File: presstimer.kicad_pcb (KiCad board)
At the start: 4 copper layers, 93 x 72 mm, 87 parts, among them J1 Screw_Terminal_01x02, J10 Screw_Terminal_01x02, J11 Connector, USB-TYPE-C-16P, J2 Screw_Terminal_01x03, J3 Connector, USB-TYPE-C-16P, J4 Conn_ARM_SWD_TagConnect_TC2030, J5 Conn_01x06_Pin, J6 Conn_01x06_Pin, J8 Screw_Terminal_01x02, J9 Screw_Terminal_01x02, Q10 L8050QLT1G, Q5 Display 2.8" TFT LCD Touch IL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, Q6 AO3401A, Q8 L8050QLT1G, Q9 L8050QLT1G, SW1 SW_Push, SW2 SW_Push, U1 AP7361C-33ER, U2 ESP32-S3-WROOM-1, U3 SFH620A-3X001, U4 SFH620A-3X001, U5 SSR-41FDD, U6 CP2102N-Axx-xQFN28

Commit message: fix: corrected 3v3 connections at D5, USB power to LDO, power to I2C expansion
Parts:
- renumbered TP2 to 3V3, TP1 to 5V, TP4 to 5V, TP6 to 5V, SW1 to BOOT, TP7 to GND, TP3 to GND, TP5 to GND, SW2 to RESET
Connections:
- C10 pad 1: USB2_5V -> +5V
- C11 pad 1: USB_5V -> +5V
- C2 pad 1: Net-(D1-A) -> +3V3
- D1 pad 1: +3V3 -> Net-(D1-K)
- D1 pad 2: Net-(D1-A) -> +3V3
- D5 pad 1: USB_5V -> +5V
- D6 pad 1: USB2_5V -> +5V
- R3 pad 1: +3V3 -> Net-(D1-K)
- U1 pad 2: Net-(D1-A) -> +3V3
- U1 pad 4: Net-(D1-A) -> +3V3
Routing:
- net +5V: track 76.5 -> 172.6 mm, vias 1 -> 7
- net +3V3: track 221.8 -> 258.7 mm
- net Net-(D1-A): track 15.5 -> 0.00 mm
- net VBUSB2: track 21.0 -> 16.7 mm
- net Net-(D1-K): track 0.00 -> 2.36 mm
- net USB_5V: track 2.29 -> 0.00 mm
- net USB2_5V: track 2.26 -> 0.00 mm

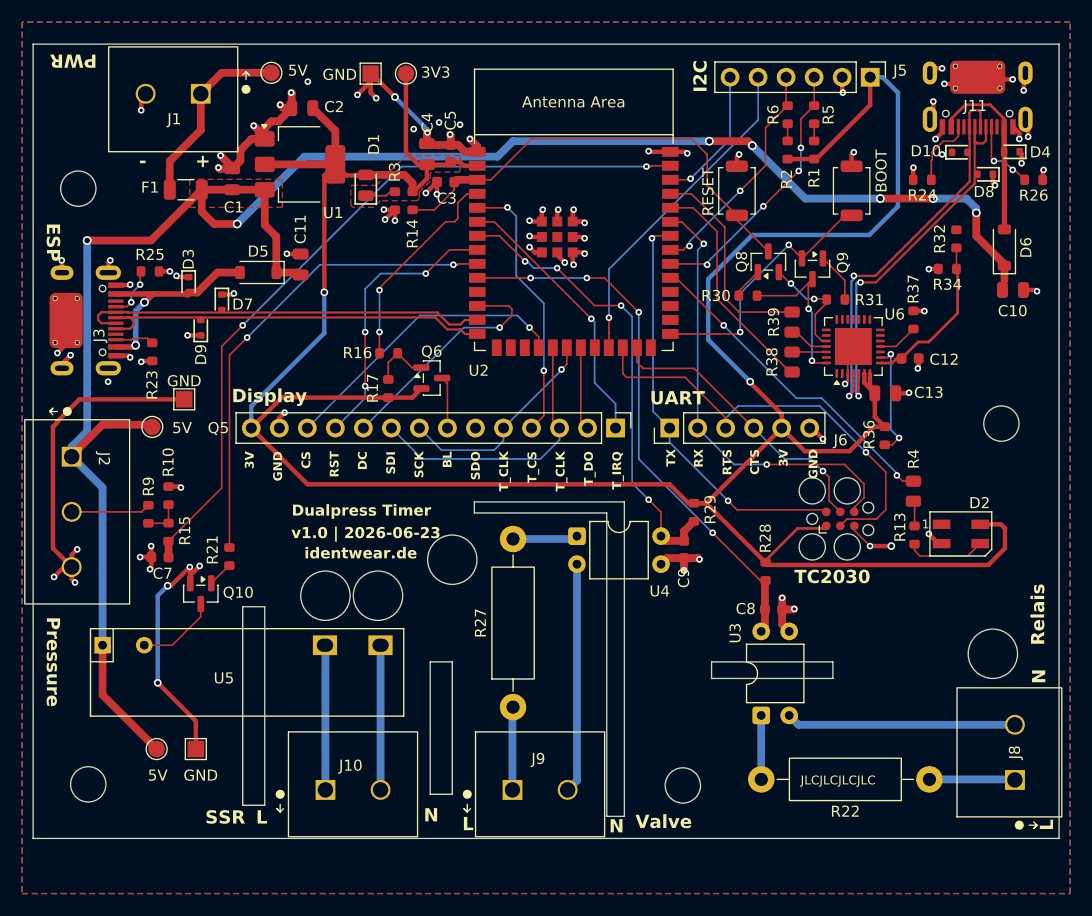
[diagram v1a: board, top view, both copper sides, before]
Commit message: fixed ssr pinout
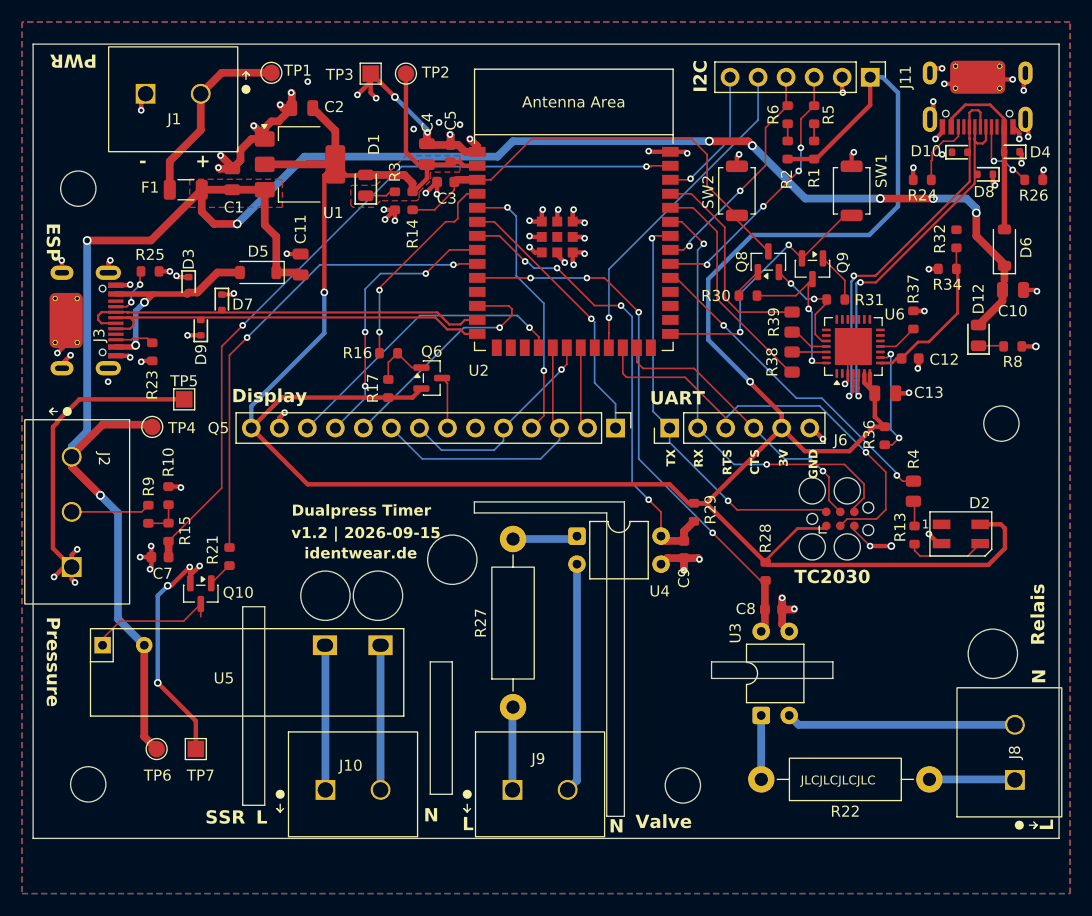
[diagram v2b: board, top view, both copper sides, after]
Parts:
- added D12: LED, PCM_JLCPCB:D_0805, F.Cu at (184.7, 106.4)
- added R8: 1k, PCM_JLCPCB:R_0603, F.Cu at (187.8, 107.4)
- renumbered BOOT to SW1, RESET to SW2, 5V to TP1, 3V3 to TP2, GND to TP3, 5V to TP4, GND to TP5, 5V to TP6, GND to TP7
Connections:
- U5 pad 1: +5V -> Net-(J10-Pin_1)
- U5 pad 2: Net-(Q10-C) -> Net-(J10-Pin_2)
- U5 pad 3: Net-(J10-Pin_1) -> +5V
- U5 pad 4: Net-(J10-Pin_2) -> Net-(Q10-C)
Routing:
- net Net-(Q10-C): track 7.35 -> 11.9 mm
- net +5V: track 172.6 -> 176.7 mm, vias 7 -> 8
- net Net-(D12-K): track 0.00 -> 2.30 mm
- net GND: track 186.8 -> 188.1 mm, vias 89 -> 90
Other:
- board text added: "v1.2 | 2026-09-15"
- board text added: "зайка"
- board text removed: "v1.0 | 2026-06-23"

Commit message: before removal of cp2102
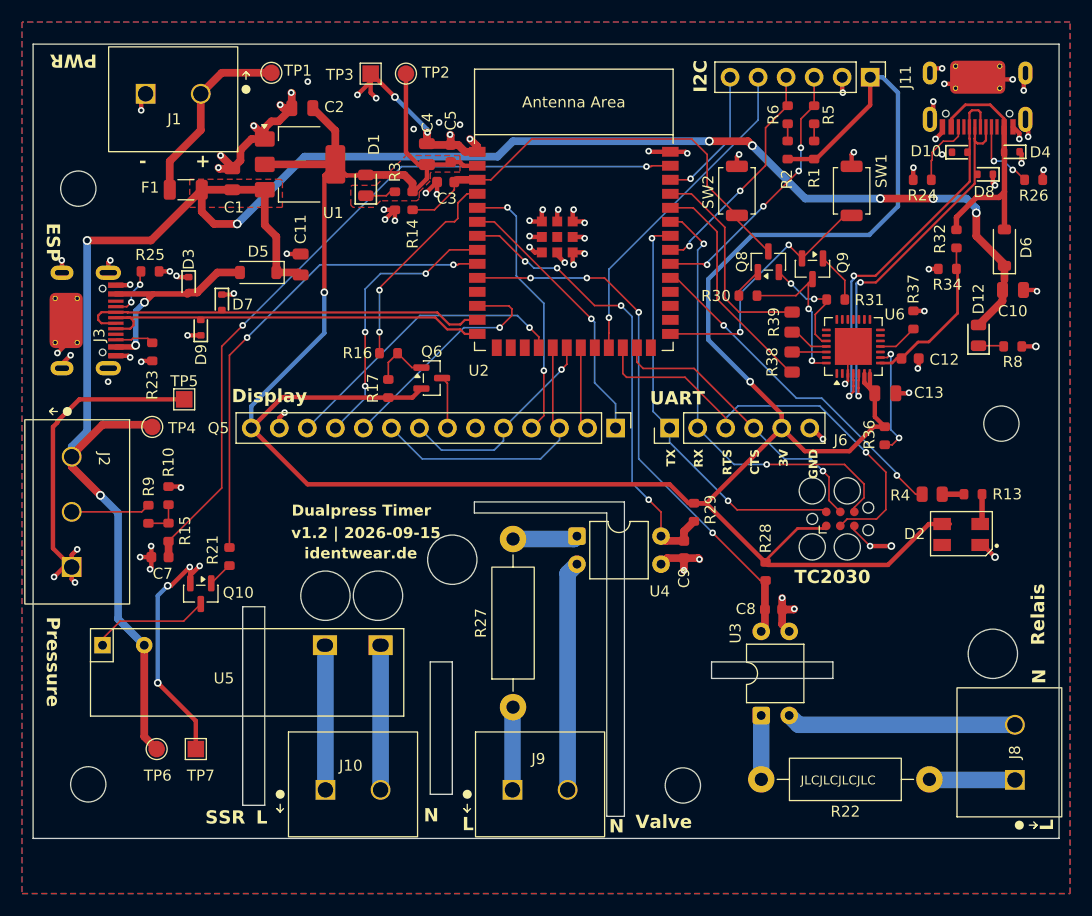
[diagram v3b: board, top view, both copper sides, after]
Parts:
- D2: footprint LED_SMD:LED_SK6812MINI_PLCC4_3.5x3.5mm_P1.75mm -> markus:SK6812MINI--HS-012_3.7x3.5mm
- moved R13 6.46 mm to (184.2, 120.8), turned to 0 degrees
- moved D2 1.92 mm to (181.4, 123.5)
- moved R4 1.72 mm to (180.5, 120.8), turned to 0 degrees
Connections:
- D2 pad 1: unconnected-(D2-DOUT-Pad1) -> GND
- D2 pad 2: GND -> Net-(D2-DIN)
- D2 pad 3: Net-(D2-DIN) -> +3V3
- D2 pad 4: +3V3 -> unconnected-(D2-DOUT-Pad4)
- U5 pad 1: Net-(J10-Pin_1) -> Net-(J10-Pin_2)
- U5 pad 2: Net-(J10-Pin_2) -> Net-(J10-Pin_1)
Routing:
- net +3V3: track 258.7 -> 250.4 mm
- net VBUSB2: track 16.7 -> 23.1 mm
- net Net-(D2-DIN): track 7.20 -> 2.98 mm
- net LED_RGB: track 29.8 -> 31.1 mm
- net Net-(Q10-C): track 11.9 -> 10.8 mm
- net GND: track 188.1 -> 188.7 mm

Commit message: add: connector heating SSR
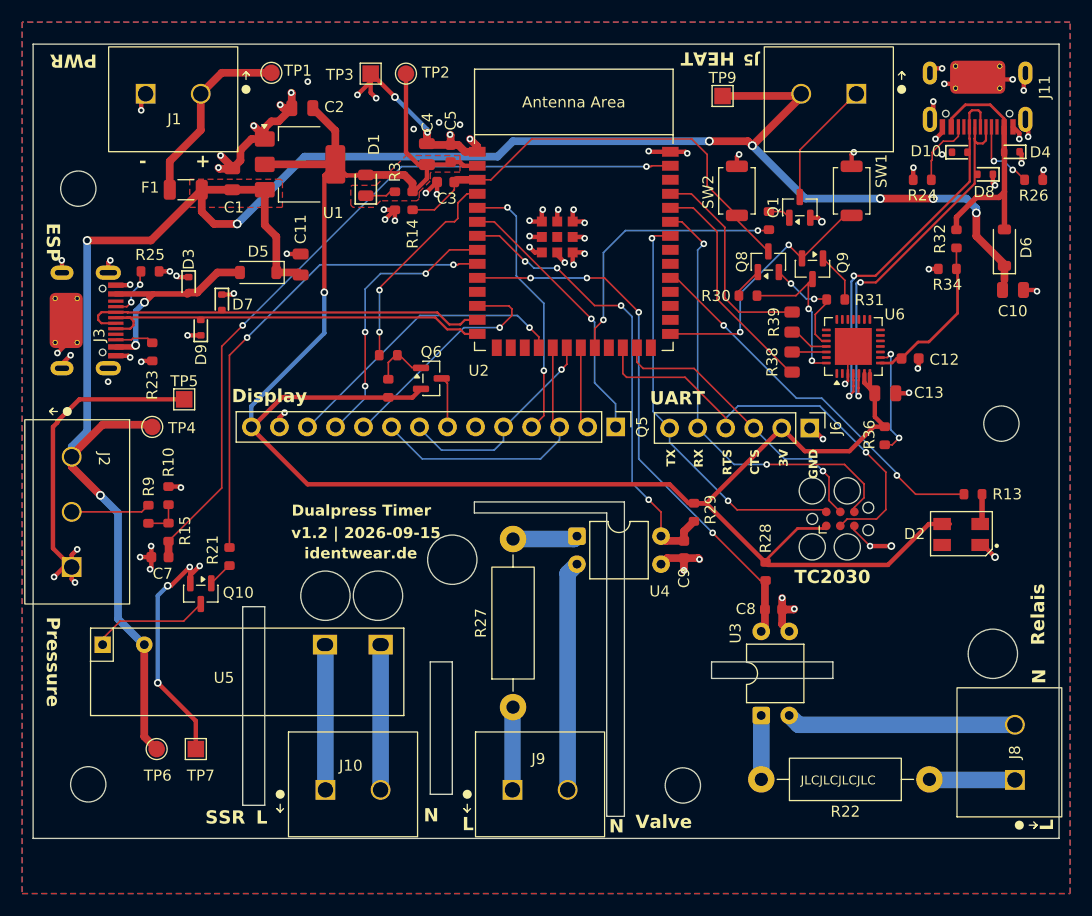
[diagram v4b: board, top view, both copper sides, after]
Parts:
- removed D12: LED, PCM_JLCPCB:D_0805
- removed R2: 4k7, PCM_JLCPCB:R_0603
- removed R37: 10k, PCM_JLCPCB:R_0603
- removed R4: 0, PCM_JLCPCB:R_0805
- removed R5, R6: 0, PCM_JLCPCB:R_0603
- removed R8: 1k, PCM_JLCPCB:R_0603
- added Q1: L8050QLT1G, Package_TO_SOT_SMD:SOT-23, F.Cu at (168.5, 94.8)
- added TP9: TestPoint, TestPoint:TestPoint_Pad_1.5x1.5mm, F.Cu at (161.5, 84.7)
- J5: value Conn_01x06_Pin -> Screw_Terminal_01x02; footprint Connector_PinHeader_2.54mm:PinHeader_1x06_P2.54mm_Vertical -> markus:DG305-5.0-02P-12-00A(H)
- R1: value 4k7 -> 1k
- U5: value SSR-41FDD -> SSR-41FDA
- moved J6 12.7 mm to (169.4, 114.8), turned to -90 degrees
- moved R1 7.60 mm to (165.7, 96.0), turned to 90 degrees
- moved J5 6.76 mm to (176.7, 89.5), turned to 180 degrees
- moved R16 0.18 mm to (131.2, 108.2)
- moved Q5 0.10 mm to (151.8, 114.7)
- moved U5 0.05 mm to (105.3, 134.4)
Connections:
- net Net-(J10-Pin_1) renamed /Connections/SSR_L
- net Net-(J10-Pin_2) renamed /Connections/SSR_SW_L
- net Net-(J8-Pin_1) renamed /Connections/SENSE_RELAY1
- net Net-(J8-Pin_2) renamed /Connections/SENSE_RELAY2
- net Net-(J9-Pin_1) renamed /Connections/SENSE_SOLENOID1
- net Net-(J9-Pin_2) renamed /Connections/SENSE_SOLENOID2
- J5 pad 1: +3V3 -> Net-(J5-Pin_1)
- J5 pad 2: GND -> +5V
- J6 pad 1: UART_TX -> GND
- J6 pad 2: UART_RX -> +3V3
- J6 pad 3: UART_RTS -> UART_CTS
- J6 pad 4: UART_CTS -> UART_RTS
- J6 pad 5: +3V3 -> UART_RX
- J6 pad 6: GND -> UART_TX
- R1 pad 1: Net-(R1-Pad1) -> GPIO14
- R1 pad 2: +3V3 -> Net-(Q1-B)
- R13 pad 1: Net-(R13-Pad1) -> LED_RGB
- U2 pad 23: I2C_INT -> GPIO21
- U2 pad 32: I2C_SDA -> GPIO39
- U2 pad 33: I2C_SCL -> GPIO40
- U2 pad 38: I2C_RST -> GPIO2
- U6 pad 11: Net-(U6-~{SUSPEND}) -> unconnected-(U6-~{SUSPEND}-Pad11)
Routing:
- net +3V3: track 250.4 -> 188.8 mm, vias 2 -> 1
- net I2C_INT: track 30.1 -> 0.00 mm, vias 1 -> 0
- net GPIO14: track 0.00 -> 24.8 mm, vias 0 -> 2
- net I2C_SDA: track 24.4 -> 0.00 mm, vias 4 -> 0
- net I2C_SCL: track 20.9 -> 0.00 mm, vias 2 -> 0
- net I2C_RST: track 12.6 -> 0.00 mm, vias 1 -> 0
- net Net-(J5-Pin_1): track 0.00 -> 11.5 mm
- net +5V: track 176.7 -> 186.3 mm
- net LED_RGB: track 31.1 -> 34.9 mm
- net Net-(U6-~{SUSPEND}): track 3.65 -> 0.00 mm
- net GND: track 188.7 -> 186.2 mm, vias 90 -> 88
- net Net-(D12-K): track 2.30 -> 0.00 mm
- net Net-(Q1-B): track 0.00 -> 2.08 mm
- net Net-(R13-Pad1): track 1.97 -> 0.00 mm
- net Net-(R2-Pad2): track 1.56 -> 0.00 mm
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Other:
- board text added: "HEAT"
- board text removed: "I2C"
